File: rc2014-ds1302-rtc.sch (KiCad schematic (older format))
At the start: 18 parts, among them P1 RC2014 BUS, SW1 SW_DIP_x06, U1 74HCT688, U2 74LS125, U3 74LS174, U4 DS1302, U5 74LS32, U6 74LS125, Y1 Crystal

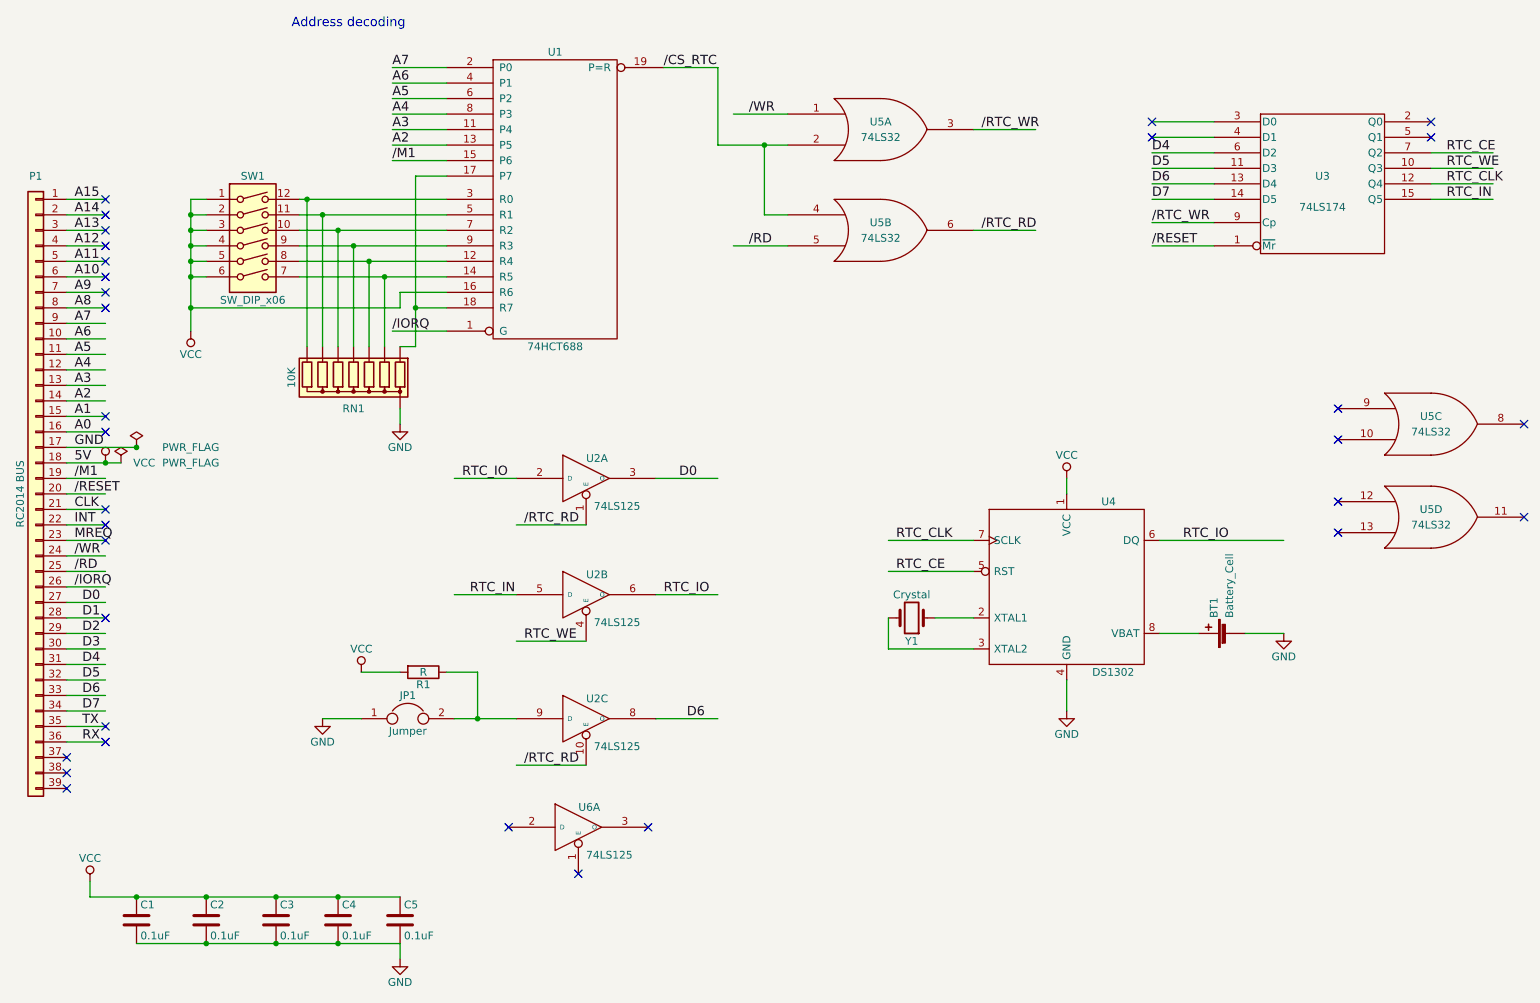
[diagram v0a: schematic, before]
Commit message: start pcb layout
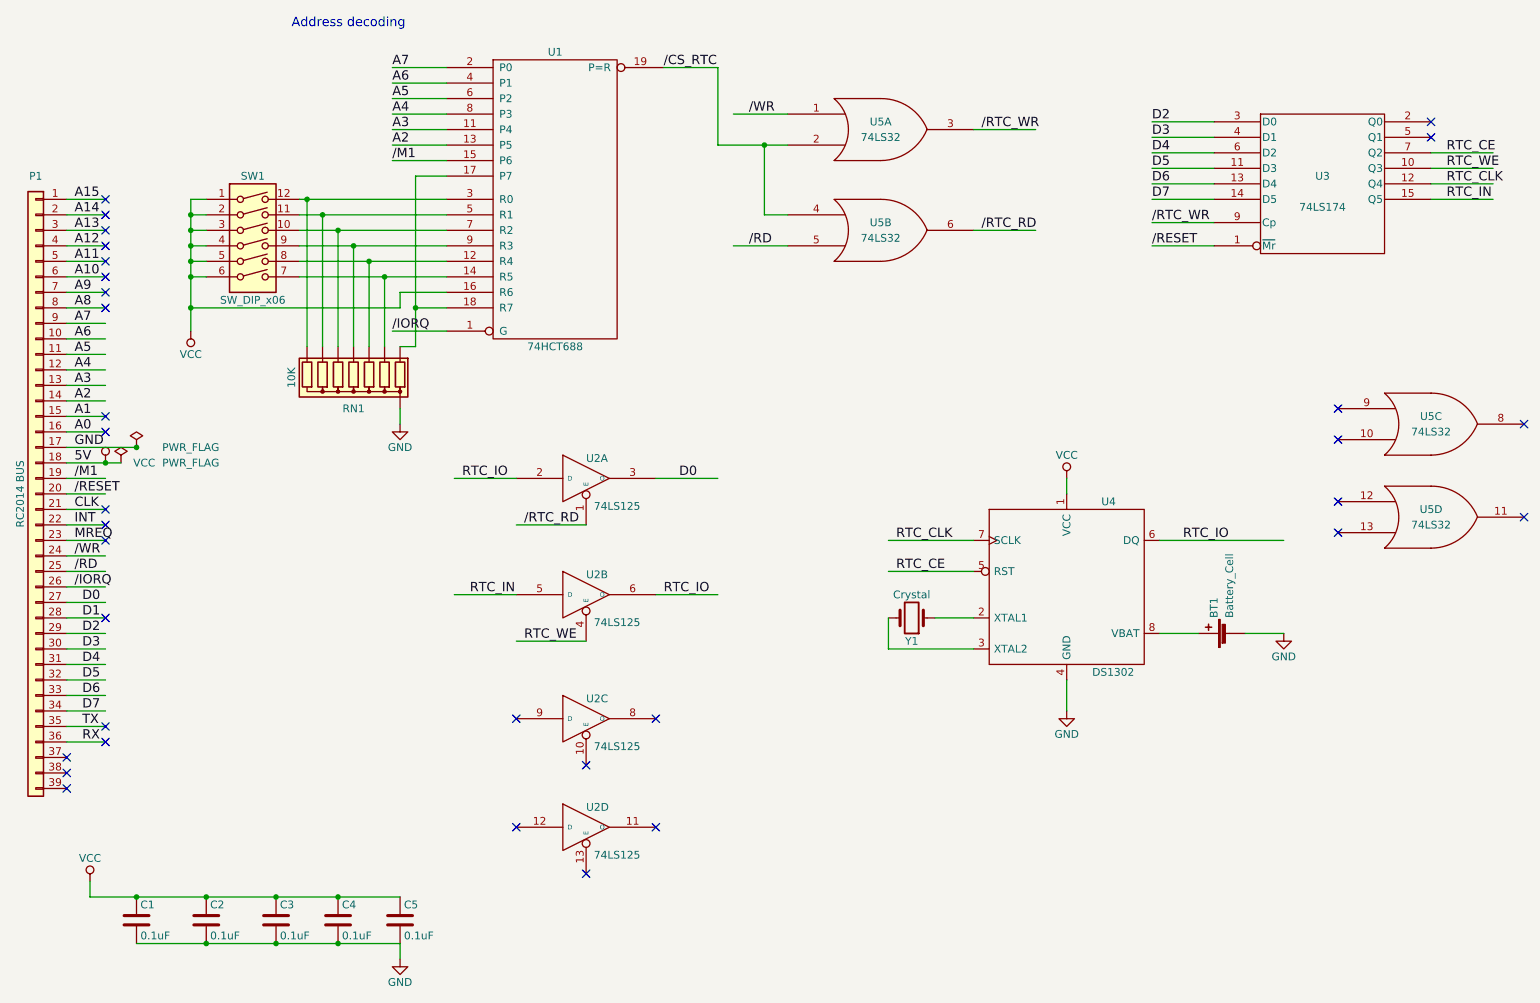
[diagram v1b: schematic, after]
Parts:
- removed JP1: Jumper, symbol Jumper
- removed R1: R, symbol R
- removed U6: 74LS125, symbol 74LS125
- added unit 4 of U2
- BT1: footprint Battery_Holders:Keystone_1058_1x2032-CoinCell -> Battery_Holders:Keystone_106_1x20mm-CoinCell
- U2: footprint Housings_DIP:DIP-14_W7.62mm_Socket -> Housings_DIP:DIP-14_W7.62mm_Socket_LongPads
- U3: footprint Housings_DIP:DIP-16_W7.62mm_Socket -> Housings_DIP:DIP-16_W7.62mm_Socket_LongPads
- U4: footprint Housings_DIP:DIP-8_W7.62mm_Socket -> Housings_DIP:DIP-8_W7.62mm_Socket_LongPads
- U5: footprint Housings_DIP:DIP-8_W7.62mm_Socket -> Housings_DIP:DIP-14_W7.62mm_Socket_LongPads
- U5: footprint (none) -> Housings_DIP:DIP-14_W7.62mm_Socket_LongPads
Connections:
- wire segments 119 -> 112
- no-connect marks 32 -> 33
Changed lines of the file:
@@
 EESchema Schematic File Version 2
-LIBS:rc2014-ds1302-rtc-rescue
+LIBS:rc2014-ds1302-rtc
 LIBS:power
 LIBS:device
@@
 F 0 "U4" H 7820 4850 50  0000 C CNN
 F 1 "DS1302" H 7850 3750 50  0000 C CNN
-F 2 "Housings_DIP:DIP-8_W7.62mm_Socket" H 7550 4300 50  0001 C CNN
+F 2 "Housings_DIP:DIP-8_W7.62mm_Socket_LongPads" H 7550 4300 50  0001 C CNN
 F 3 "" H 7550 4300 50  0001 C CNN
 	1    7550 4300
@@
 F 0 "BT1" H 8700 4700 50  0000 L CNN
 F 1 "Battery_Cell" H 8700 4600 50  0000 L CNN
-F 2 "Battery_Holders:Keystone_1058_1x2032-CoinCell" V 8600 4660 50  0001 C CNN
+F 2 "Battery_Holders:Keystone_106_1x20mm-CoinCell" V 8600 4660 50  0001 C CNN
 F 3 "" V 8600 4660 50  0001 C CNN
 	1    8600 4600
@@
 F 0 "U2" H 4450 3700 50  0000 L BNN
 F 1 "74LS125" H 4500 3450 50  0000 L TNN
-F 2 "Housings_DIP:DIP-14_W7.62mm_Socket" H 4450 3600 50  0001 C CNN
+F 2 "Housings_DIP:DIP-14_W7.62mm_Socket_LongPads" H 4450 3600 50  0001 C CNN
 F 3 "" H 4450 3600 50  0001 C CNN
 	1    4450 3600
@@
 F 0 "U2" H 4450 4450 50  0000 L BNN
 F 1 "74LS125" H 4500 4200 50  0000 L TNN
-F 2 "Housings_DIP:DIP-14_W7.62mm_Socket" H 4450 4350 50  0001 C CNN
+F 2 "Housings_DIP:DIP-14_W7.62mm_Socket_LongPads" H 4450 4350 50  0001 C CNN
 F 3 "" H 4450 4350 50  0001 C CNN
 	2    4450 4350
@@
 F 0 "U3" H 9200 1750 50  0000 C CNN
 F 1 "74LS174" H 9200 1550 50  0000 C CNN
-F 2 "Housings_DIP:DIP-16_W7.62mm_Socket" H 9200 1700 50  0001 C CNN
+F 2 "Housings_DIP:DIP-16_W7.62mm_Socket_LongPads" H 9200 1700 50  0001 C CNN
 F 3 "" H 9200 1700 50  0001 C CNN
 	1    9200 1700
@@
 F 0 "U2" H 4450 5250 50  0000 L BNN
 F 1 "74LS125" H 4500 5000 50  0000 L TNN
-F 2 "Housings_DIP:DIP-14_W7.62mm_Socket" H 4450 5150 50  0001 C CNN
+F 2 "Housings_DIP:DIP-14_W7.62mm_Socket_LongPads" H 4450 5150 50  0001 C CNN
 F 3 "" H 4450 5150 50  0001 C CNN
 	3    4450 5150
@@
 	4900 4350 5300 4350
 Wire Wire Line
-	4900 5150 5300 5150
-Wire Wire Line
 	3600 3600 4000 3600
 Wire Wire Line
 	3600 4350 4000 4350
 Wire Wire Line
-	3600 5150 4000 5150
-Wire Wire Line
 	4450 3900 4000 3900
 Wire Wire Line
 	4450 4650 4000 4650
-Wire Wire Line
-	4450 5450 4000 5450
 Text Label 5050 3600 0    60   ~ 0
 D0
 Text Label 4950 4350 0    60   ~ 0
 RTC_IO
-Text Label 5100 5150 0    60   ~ 0
-D6
 Text Label 4050 3900 0    60   ~ 0
 /RTC_RD
 Text Label 4050 4650 0    60   ~ 0
 RTC_WE
-Text Label 4050 5450 0    60   ~ 0
-/RTC_RD
 Text Label 3650 3600 0    60   ~ 0
 RTC_IO
@@
 F 0 "U5" H 6350 1400 50  0000 C CNN
 F 1 "74LS32" H 6350 1300 50  0000 C CNN
-F 2 "Housings_DIP:DIP-8_W7.62mm_Socket" H 6350 1350 50  0001 C CNN
+F 2 "Housings_DIP:DIP-14_W7.62mm_Socket_LongPads" H 6350 1350 50  0001 C CNN
 F 3 "" H 6350 1350 50  0001 C CNN
 	1    6350 1350
@@
 F 0 "U5" H 6350 2050 50  0000 C CNN
 F 1 "74LS32" H 6350 1950 50  0000 C CNN
-F 2 "Housings_DIP:DIP-8_W7.62mm_Socket" H 6350 2000 50  0001 C CNN
+F 2 "Housings_DIP:DIP-14_W7.62mm_Socket_LongPads" H 6350 2000 50  0001 C CNN
 F 3 "" H 6350 2000 50  0001 C CNN
 	2    6350 2000
@@
 Connection ~ 2850 6600
 Connection ~ 2850 6300
-$Comp
-L Jumper JP1
-U 1 1 5A4D28E3
-P 3300 5150
-F 0 "JP1" H 3300 5300 50  0000 C CNN
-F 1 "Jumper" H 3300 5070 50  0000 C CNN
-F 2 "" H 3300 5150 50  0001 C CNN
-F 3 "" H 3300 5150 50  0001 C CNN
-	1    3300 5150
-	1    0    0    -1
-$EndComp
-Wire Wire Line
-	3000 5150 2750 5150
-$Comp
-L GND #PWR011
-U 1 1 5A4D2A19
-P 2750 5150
-F 0 "#PWR011" H 2750 4900 50  0001 C CNN
-F 1 "GND" H 2750 5000 50  0000 C CNN
-F 2 "" H 2750 5150 50  0001 C CNN
-F 3 "" H 2750 5150 50  0001 C CNN
-	1    2750 5150
-	1    0    0    -1
-$EndComp
-Wire Wire Line
-	3750 5150 3750 4850
-Wire Wire Line
-	3750 4850 3550 4850
-Connection ~ 3750 5150
-$Comp
-L R R1
-U 1 1 5A4D2AF5
-P 3400 4850
-F 0 "R1" V 3480 4850 50  0000 C CNN
-F 1 "R" V 3400 4850 50  0000 C CNN
-F 2 "" V 3330 4850 50  0001 C CNN
-F 3 "" H 3400 4850 50  0001 C CNN
-	1    3400 4850
-	0    1    1    0
-$EndComp
-Wire Wire Line
-	3250 4850 3000 4850
-$Comp
-L VCC #PWR012
-U 1 1 5A4D2C1E
-P 3000 4850
-F 0 "#PWR012" H 3000 4700 50  0001 C CNN
-F 1 "VCC" H 3000 5000 50  0000 C CNN
-F 2 "" H 3000 4850 50  0001 C CNN
-F 3 "" H 3000 4850 50  0001 C CNN
-	1    3000 4850
-	1    0    0    -1
-$EndComp
 NoConn ~ 1350 3200
 NoConn ~ 1350 3300
@@
 F 0 "U5" H 9900 3300 50  0000 C CNN
 F 1 "74LS32" H 9900 3200 50  0000 C CNN
-F 2 "" H 9900 3250 50  0001 C CNN
+F 2 "Housings_DIP:DIP-14_W7.62mm_Socket_LongPads" H 9900 3250 50  0001 C CNN
 F 3 "" H 9900 3250 50  0001 C CNN
 	3    9900 3250
@@
 F 0 "U5" H 9900 3900 50  0000 C CNN
 F 1 "74LS32" H 9900 3800 50  0000 C CNN
-F 2 "" H 9900 3850 50  0001 C CNN
+F 2 "Housings_DIP:DIP-14_W7.62mm_Socket_LongPads" H 9900 3850 50  0001 C CNN
 F 3 "" H 9900 3850 50  0001 C CNN
 	4    9900 3850
@@
 NoConn ~ 9300 3750
 NoConn ~ 9300 3950
-$Comp
-L 74LS125 U6
-U 1 1 5A4D38C3
-P 4400 5850
-F 0 "U6" H 4400 5950 50  0000 L BNN
-F 1 "74LS125" H 4450 5700 50  0000 L TNN
-F 2 "" H 4400 5850 50  0001 C CNN
-F 3 "" H 4400 5850 50  0001 C CNN
-	1    4400 5850
-	1    0    0    -1
-$EndComp
-NoConn ~ 3950 5850
-NoConn ~ 4400 6150
-NoConn ~ 4850 5850
+NoConn ~ 4000 5850
+NoConn ~ 4450 6150
+NoConn ~ 4900 5850
 NoConn ~ 1350 4500
 Wire Wire Line
 	5300 950  5300 1450
-NoConn ~ 8100 1300
-NoConn ~ 8100 1400
+Text Label 8100 1300 0    60   ~ 0
+D2
+Text Label 8100 1400 0    60   ~ 0
+D3
+$Comp
+L 74LS125 U2
+U 4 1 5A4D6CB2
+P 4450 5850
+F 0 "U2" H 4450 5950 50  0000 L BNN
+F 1 "74LS125" H 4500 5700 50  0000 L TNN
+F 2 "Housings_DIP:DIP-14_W7.62mm_Socket_LongPads" H 4450 5850 50  0001 C CNN
+F 3 "" H 4450 5850 50  0001 C CNN
+	4    4450 5850
+	1    0    0    -1
+$EndComp
+NoConn ~ 4000 5150
+NoConn ~ 4450 5450
+NoConn ~ 4900 5150
 $EndSCHEMATC

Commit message: Think this is ready for manufacturing...
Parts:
- U2: value 74LS125 -> 74HCT125
- U3: value 74LS174 -> 74HCT174
- U5: value 74LS32 -> 74HCT32
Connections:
- wire segments 112 -> 117
- no-connect marks 33 -> 25
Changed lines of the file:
@@
 LIBS:contrib
 LIBS:valves
-LIBS:jumper_dual
 LIBS:switches
 LIBS:maxim
@@
 Sheet 1 1
 Title "RC2014 DS1302 RTC"
-Date "2018-01-02"
+Date "2018-01-21"
 Rev "2"
 Comp "Ed Brindley"
@@
 P 4450 3600
 F 0 "U2" H 4450 3700 50  0000 L BNN
-F 1 "74LS125" H 4500 3450 50  0000 L TNN
+F 1 "74HCT125" H 4500 3450 50  0000 L TNN
 F 2 "Housings_DIP:DIP-14_W7.62mm_Socket_LongPads" H 4450 3600 50  0001 C CNN
 F 3 "" H 4450 3600 50  0001 C CNN
@@
 P 4450 4350
 F 0 "U2" H 4450 4450 50  0000 L BNN
-F 1 "74LS125" H 4500 4200 50  0000 L TNN
+F 1 "74HCT125" H 4500 4200 50  0000 L TNN
 F 2 "Housings_DIP:DIP-14_W7.62mm_Socket_LongPads" H 4450 4350 50  0001 C CNN
 F 3 "" H 4450 4350 50  0001 C CNN
@@
 P 9200 1700
 F 0 "U3" H 9200 1750 50  0000 C CNN
-F 1 "74LS174" H 9200 1550 50  0000 C CNN
+F 1 "74HCT174" H 9200 1550 50  0000 C CNN
 F 2 "Housings_DIP:DIP-16_W7.62mm_Socket_LongPads" H 9200 1700 50  0001 C CNN
 F 3 "" H 9200 1700 50  0001 C CNN
@@
 P 4450 5150
 F 0 "U2" H 4450 5250 50  0000 L BNN
-F 1 "74LS125" H 4500 5000 50  0000 L TNN
+F 1 "74HCT125" H 4500 5000 50  0000 L TNN
 F 2 "Housings_DIP:DIP-14_W7.62mm_Socket_LongPads" H 4450 5150 50  0001 C CNN
 F 3 "" H 4450 5150 50  0001 C CNN
@@
 P 6350 1350
 F 0 "U5" H 6350 1400 50  0000 C CNN
-F 1 "74LS32" H 6350 1300 50  0000 C CNN
+F 1 "74HCT32" H 6350 1300 50  0000 C CNN
 F 2 "Housings_DIP:DIP-14_W7.62mm_Socket_LongPads" H 6350 1350 50  0001 C CNN
 F 3 "" H 6350 1350 50  0001 C CNN
@@
 P 6350 2000
 F 0 "U5" H 6350 2050 50  0000 C CNN
-F 1 "74LS32" H 6350 1950 50  0000 C CNN
+F 1 "74HCT32" H 6350 1950 50  0000 C CNN
 F 2 "Housings_DIP:DIP-14_W7.62mm_Socket_LongPads" H 6350 2000 50  0001 C CNN
 F 3 "" H 6350 2000 50  0001 C CNN
@@
 P 9900 3250
 F 0 "U5" H 9900 3300 50  0000 C CNN
-F 1 "74LS32" H 9900 3200 50  0000 C CNN
+F 1 "74HCT32" H 9900 3200 50  0000 C CNN
 F 2 "Housings_DIP:DIP-14_W7.62mm_Socket_LongPads" H 9900 3250 50  0001 C CNN
 F 3 "" H 9900 3250 50  0001 C CNN
@@
 P 9900 3850
 F 0 "U5" H 9900 3900 50  0000 C CNN
-F 1 "74LS32" H 9900 3800 50  0000 C CNN
+F 1 "74HCT32" H 9900 3800 50  0000 C CNN
 F 2 "Housings_DIP:DIP-14_W7.62mm_Socket_LongPads" H 9900 3850 50  0001 C CNN
 F 3 "" H 9900 3850 50  0001 C CNN
@@
 NoConn ~ 10500 3250
 NoConn ~ 10500 3850
-NoConn ~ 9300 3150
-NoConn ~ 9300 3350
-NoConn ~ 9300 3750
-NoConn ~ 9300 3950
-NoConn ~ 4000 5850
-NoConn ~ 4450 6150
 NoConn ~ 4900 5850
 NoConn ~ 1350 4500
@@
 Text Label 8100 1400 0    60   ~ 0
 D3
+NoConn ~ 4900 5150
 $Comp
 L 74LS125 U2
@@
 P 4450 5850
 F 0 "U2" H 4450 5950 50  0000 L BNN
-F 1 "74LS125" H 4500 5700 50  0000 L TNN
+F 1 "74HCT125" H 4500 5700 50  0000 L TNN
 F 2 "Housings_DIP:DIP-14_W7.62mm_Socket_LongPads" H 4450 5850 50  0001 C CNN
 F 3 "" H 4450 5850 50  0001 C CNN
@@
 	1    0    0    -1
 $EndComp
-NoConn ~ 4000 5150
-NoConn ~ 4450 5450
-NoConn ~ 4900 5150
+$Comp
+L GND #PWR?
+U 1 1 5A649171
+P 4000 5150
+F 0 "#PWR?" H 4000 4900 50  0001 C CNN
+F 1 "GND" H 4000 5000 50  0000 C CNN
+F 2 "" H 4000 5150 50  0001 C CNN
+F 3 "" H 4000 5150 50  0001 C CNN
+	1    4000 5150
+	1    0    0    -1
+$EndComp
+$Comp
+L GND #PWR?
+U 1 1 5A6491AF
+P 4000 5850
+F 0 "#PWR?" H 4000 5600 50  0001 C CNN
+F 1 "GND" H 4000 5700 50  0000 C CNN
+F 2 "" H 4000 5850 50  0001 C CNN
+F 3 "" H 4000 5850 50  0001 C CNN
+	1    4000 5850
+	1    0    0    -1
+$EndComp
+$Comp
+L GND #PWR?
+U 1 1 5A6491ED
+P 4450 5450
+F 0 "#PWR?" H 4450 5200 50  0001 C CNN
+F 1 "GND" H 4450 5300 50  0000 C CNN
+F 2 "" H 4450 5450 50  0001 C CNN
+F 3 "" H 4450 5450 50  0001 C CNN
+	1    4450 5450
+	1    0    0    -1
+$EndComp
+$Comp
+L GND #PWR?
+U 1 1 5A64922B
+P 4450 6150
+F 0 "#PWR?" H 4450 5900 50  0001 C CNN
+F 1 "GND" H 4450 6000 50  0000 C CNN
+F 2 "" H 4450 6150 50  0001 C CNN
+F 3 "" H 4450 6150 50  0001 C CNN
+	1    4450 6150
+	1    0    0    -1
+$EndComp
+Wire Wire Line
+	9300 3150 9150 3150
+Wire Wire Line
+	9150 3150 9150 4100
+Wire Wire Line
+	9300 3350 9150 3350
+Connection ~ 9150 3350
+Wire Wire Line
+	9300 3750 9150 3750
+Connection ~ 9150 3750
+Wire Wire Line
+	9300 3950 9150 3950
+Connection ~ 9150 3950
+$Comp
+L GND #PWR?
+U 1 1 5A6494F2
+P 9150 4100
+F 0 "#PWR?" H 9150 3850 50  0001 C CNN
+F 1 "GND" H 9150 3950 50  0000 C CNN
+F 2 "" H 9150 4100 50  0001 C CNN
+F 3 "" H 9150 4100 50  0001 C CNN
+	1    9150 4100
+	1    0    0    -1
+$EndComp
 $EndSCHEMATC
